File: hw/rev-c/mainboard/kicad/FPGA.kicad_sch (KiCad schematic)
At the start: 46 parts, among them J17 PMOD1, J18 PMOD2, J19 PROG, J4 BUS_EXPANSION, J9 FPGA_MCU, Q1 MMBT3904, SW3 CONFIG, U10 T8Q144C3

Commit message: hw: update more footprints
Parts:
- U10: footprint SnapEDA:QFP50P2200X2200X160-144N -> Package_QFP:LQFP-144_20x20mm_P0.5mm
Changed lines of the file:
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@@
 			)
 		)
-		(property "Footprint" "SnapEDA:QFP50P2200X2200X160-144N"
+		(property "Footprint" "Package_QFP:LQFP-144_20x20mm_P0.5mm"
 			(at 279.4 165.1 0)
 			(effects
@@
 			)
 		)
-		(property "Footprint" "SnapEDA:QFP50P2200X2200X160-144N"
+		(property "Footprint" "Package_QFP:LQFP-144_20x20mm_P0.5mm"
 			(at 180.34 149.86 0)
 			(effects
@@
 			)
 		)
-		(property "Footprint" "SnapEDA:QFP50P2200X2200X160-144N"
+		(property "Footprint" "Package_QFP:LQFP-144_20x20mm_P0.5mm"
 			(at 278.13 143.51 0)
 			(effects
@@
 			)
 		)
-		(property "Footprint" "SnapEDA:QFP50P2200X2200X160-144N"
+		(property "Footprint" "Package_QFP:LQFP-144_20x20mm_P0.5mm"
 			(at 181.61 107.95 0)
 			(effects
@@
 			)
 		)
-		(property "Footprint" "SnapEDA:QFP50P2200X2200X160-144N"
+		(property "Footprint" "Package_QFP:LQFP-144_20x20mm_P0.5mm"
 			(at 273.05 195.58 0)
 			(effects
@@
 			)
 		)
-		(property "Footprint" "SnapEDA:QFP50P2200X2200X160-144N"
+		(property "Footprint" "Package_QFP:LQFP-144_20x20mm_P0.5mm"
 			(at 180.34 124.46 0)
 			(effects
@@
 			)
 		)
-		(property "Footprint" "SnapEDA:QFP50P2200X2200X160-144N"
+		(property "Footprint" "Package_QFP:LQFP-144_20x20mm_P0.5mm"
 			(at 287.02 110.49 0)
 			(effects
@@
 			)
 		)
-		(property "Footprint" "SnapEDA:QFP50P2200X2200X160-144N"
+		(property "Footprint" "Package_QFP:LQFP-144_20x20mm_P0.5mm"
 			(at 276.86 88.9 0)
 			(effects
@@
 			)
 		)
-		(property "Footprint" "SnapEDA:QFP50P2200X2200X160-144N"
+		(property "Footprint" "Package_QFP:LQFP-144_20x20mm_P0.5mm"
 			(at 82.55 57.15 0)
 			(effects
@@
 			)
 		)
-		(property "Footprint" "SnapEDA:QFP50P2200X2200X160-144N"
+		(property "Footprint" "Package_QFP:LQFP-144_20x20mm_P0.5mm"
 			(at 180.34 93.98 0)
 			(effects
@@
 			)
 		)
-		(property "Footprint" "SnapEDA:QFP50P2200X2200X160-144N"
+		(property "Footprint" "Package_QFP:LQFP-144_20x20mm_P0.5mm"
 			(at 78.74 167.64 0)
 			(effects
@@
 			)
 		)
-		(property "Footprint" "SnapEDA:QFP50P2200X2200X160-144N"
+		(property "Footprint" "Package_QFP:LQFP-144_20x20mm_P0.5mm"
 			(at 177.8 181.61 0)
 			(effects
@@
 			)
 		)
-		(property "Footprint" "SnapEDA:QFP50P2200X2200X160-144N"
+		(property "Footprint" "Package_QFP:LQFP-144_20x20mm_P0.5mm"
 			(at 278.13 129.54 0)
 			(effects

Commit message: hw: rework buck converter (wip)
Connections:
- net HOLD: now reaches J19.15 (Pin_15)
- no-connect marks 0 -> 1
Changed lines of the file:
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@@
 		(color 0 0 0 0)
 	)
+	(no_connect
+		(at 168.91 41.91)
+	)
 	(bus_entry
 		(at 425.45 120.65)
@@
 	(wire
 		(pts
-			(xy 153.67 41.91) (xy 163.83 41.91)
+			(xy 153.67 41.91) (xy 168.91 41.91)
 		)
 		(stroke
@@
 		)
 	)
+	(label "HOLD"
+		(at 167.64 41.91 180)
+		(fields_autoplaced yes)
+		(effects
+			(font
+				(size 1.27 1.27)
+			)
+			(justify right bottom)
+		)
+	)
 	(label "PMOD2_3"
 		(at 375.92 2.54 180)
@@
 			)
 		)
-		(property "Datasheet" "https://datasheet.lcsc.com/lcsc/2304140030_Samsung-Electro-Mechanics-CL10A106MA8NRNC_C96446.pdf"
+		(property "Datasheet" "https://product.samsungsem.com/mlcc/CL10A106MA8NRN.do"
 			(at 229.87 50.8 0)
 			(effects
@@
 			)
 		)
-		(property "Datasheet" "https://datasheet.lcsc.com/lcsc/2304140030_Samsung-Electro-Mechanics-CL10A106MA8NRNC_C96446.pdf"
+		(property "Datasheet" "https://product.samsungsem.com/mlcc/CL10A106MA8NRN.do"
 			(at 477.52 93.98 0)
 			(effects
@@
 			)
 		)
-		(property "Datasheet" "https://datasheet.lcsc.com/lcsc/2304140030_Samsung-Electro-Mechanics-CL10A106MA8NRNC_C96446.pdf"
+		(property "Datasheet" "https://product.samsungsem.com/mlcc/CL10A106MA8NRN.do"
 			(at 401.32 13.97 0)
 			(effects
@@
 			)
 		)
-		(property "Datasheet" "https://datasheet.lcsc.com/lcsc/2304140030_Samsung-Electro-Mechanics-CL10A106MA8NRNC_C96446.pdf"
+		(property "Datasheet" "https://product.samsungsem.com/mlcc/CL10A106MA8NRN.do"
 			(at 440.69 96.52 0)
 			(effects
@@
 			)
 		)
-		(property "Datasheet" "https://datasheet.lcsc.com/lcsc/2304140030_Samsung-Electro-Mechanics-CL10A106MA8NRNC_C96446.pdf"
+		(property "Datasheet" "https://product.samsungsem.com/mlcc/CL10A106MA8NRN.do"
 			(at 336.55 13.97 0)
 			(effects

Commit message: hw: renumber reference designators
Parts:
- renumbered J19 to J5, J9 to J6, J17 to J7, J18 to J8, J4 to J9, R17 to R22, R18 to R23, R19 to R24, R20 to R25, R21 to R26, R22 to R27, RN9 to RN1, RN10 to RN2

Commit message: hw: match original PET designators for connectors
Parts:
- renumbered C38 to C39, C39 to C40, C40 to C41, C41 to C42, C42 to C43, C43 to C44, C44 to C45, C45 to C46, C46 to C47, C47 to C48, C48 to C49, C49 to C50, C50 to C51, C51 to C52, C52 to C53, C53 to C54, C54 to C55, C55 to C56, C56 to C57, C57 to C58, C58 to C59, C59 to C60, C60 to C61, C61 to C62, C62 to C63, C63 to C64, C64 to C65, C65 to C66, J7 to J17, J8 to J18, J5 to J22, J9 to J4, J6 to J9, R22 to R24, R23 to R25, R24 to R26, R25 to R27, R26 to R28, R27 to R29, RN2 to RN10, RN1 to RN9

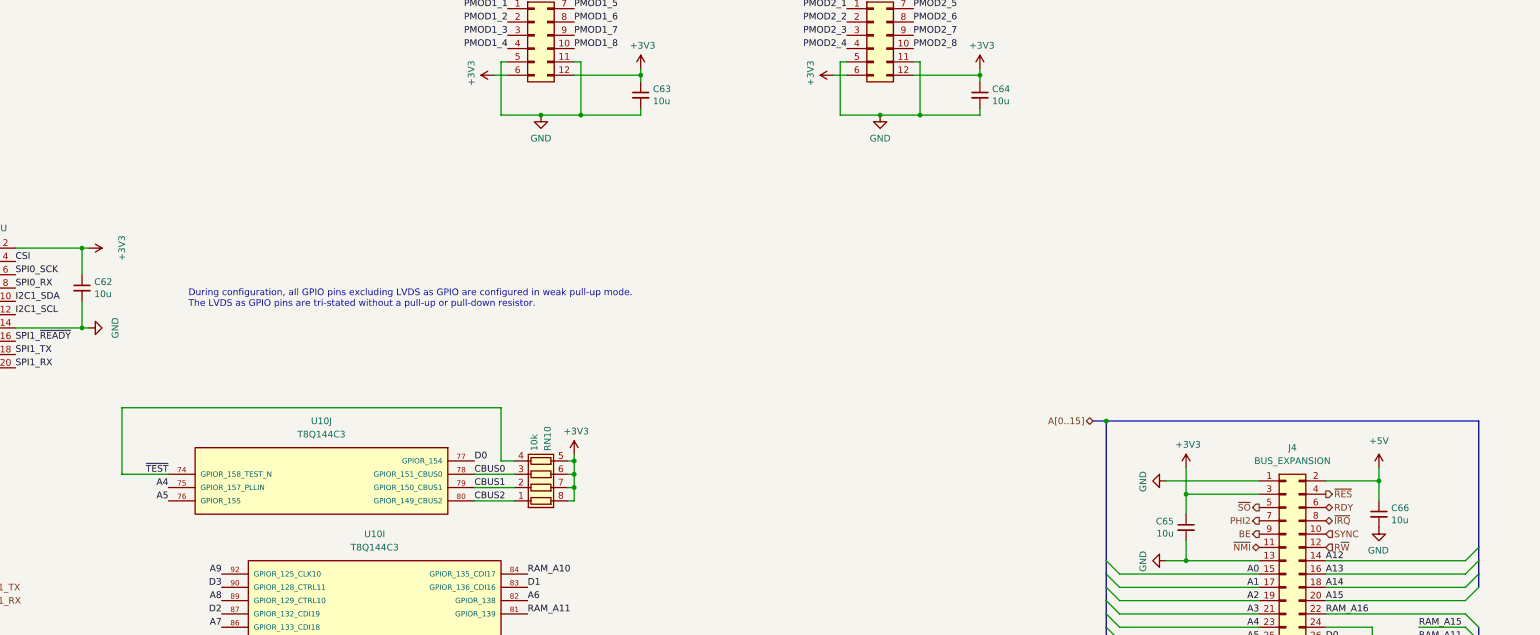
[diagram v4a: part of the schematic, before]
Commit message: hw: reduce some 3v3 decoupling caps to 4u7
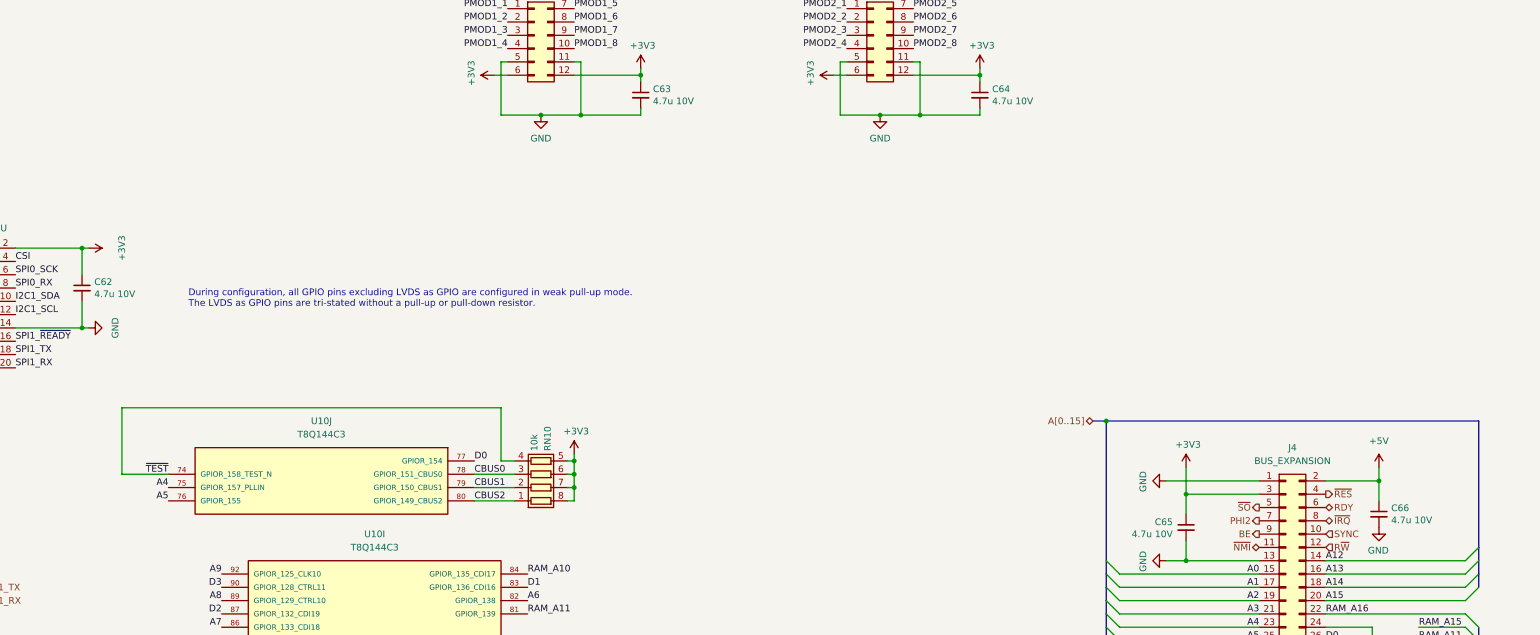
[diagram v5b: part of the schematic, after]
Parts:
- C62, C63, C64, C65, C66: value 10u -> 4.7u 10V; footprint Capacitor_SMD:C_0603_1608Metric -> Capacitor_SMD:C_0402_1005Metric; LCSC C96446 -> C23733

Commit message: hw: config can be solder jumper
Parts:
- SW3: footprint Button_Switch_THT:SW_DIP_SPSTx02_Slide_6.7x6.64mm_W7.62mm_P2.54mm_LowProfile -> EconoPET:SW_DIP_SPSTx02_Slide_6.7x6.64mm_W7.62mm_P2.54mm_LowProfile_or_SolderJumper
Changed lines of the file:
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@@
 			)
 		)
-		(property "Footprint" "Button_Switch_THT:SW_DIP_SPSTx02_Slide_6.7x6.64mm_W7.62mm_P2.54mm_LowProfile"
+		(property "Footprint" "EconoPET:SW_DIP_SPSTx02_Slide_6.7x6.64mm_W7.62mm_P2.54mm_LowProfile_or_SolderJumper"
 			(at 386.08 194.31 0)
 			(effects

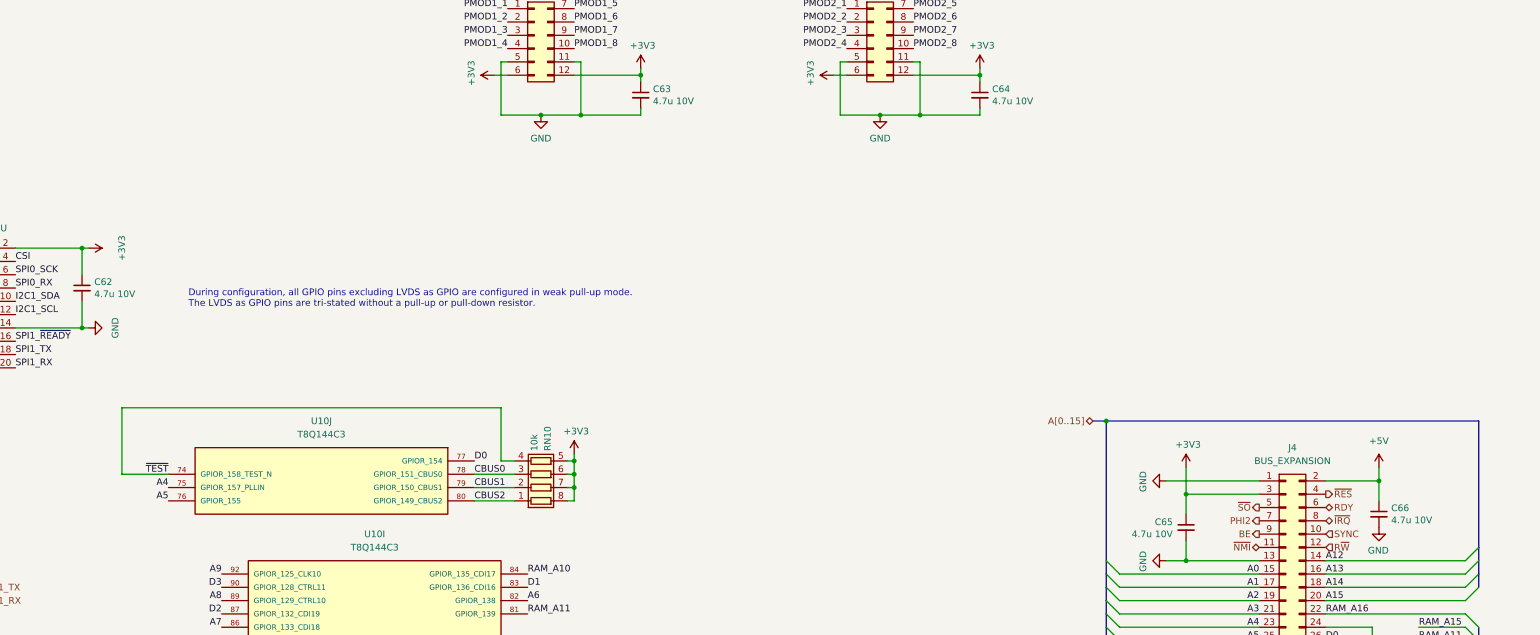
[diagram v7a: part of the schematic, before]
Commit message: hw: routing touchups, killer poke mitigation
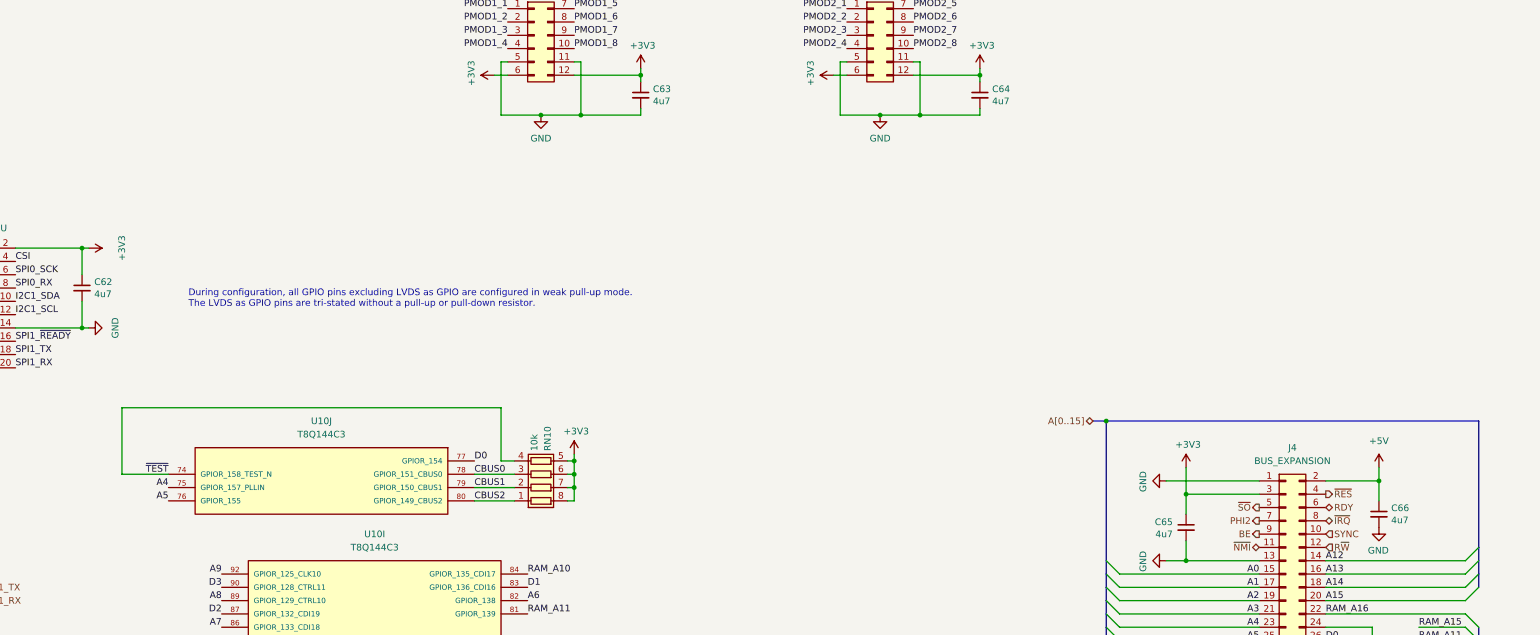
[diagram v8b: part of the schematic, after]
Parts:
- C62, C63, C64, C65, C66: value 4.7u 10V -> 4u7; LCSC C23733 -> C1538
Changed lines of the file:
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@@
 			)
 		)
-		(property "Value" "4.7u 10V"
+		(property "Value" "4u7"
 			(at 438.15 97.79 0)
 			(effects
@@
 			)
 		)
-		(property "Datasheet" "https://product.samsungsem.com/mlcc/CL05A475MP5NRN.do"
+		(property "Datasheet" "https://www.lcsc.com/datasheet/lcsc_datasheet_2304140030_FH--Guangdong-Fenghua-Advanced-Tech-0402B472K500NT_C1538.pdf"
 			(at 440.69 96.52 0)
 			(effects
@@
 			)
 		)
-		(property "LCSC" "C23733"
+		(property "LCSC" "C1538"
 			(at 440.69 96.52 0)
 			(effects
@@
 			)
 		)
-		(property "Value" "4.7u 10V"
+		(property "Value" "4u7"
 			(at 232.2068 51.943 0)
 			(effects
@@
 			)
 		)
-		(property "Datasheet" "https://product.samsungsem.com/mlcc/CL05A475MP5NRN.do"
+		(property "Datasheet" "https://www.lcsc.com/datasheet/lcsc_datasheet_2304140030_FH--Guangdong-Fenghua-Advanced-Tech-0402B472K500NT_C1538.pdf"
 			(at 229.87 50.8 0)
 			(effects
@@
 			)
 		)
-		(property "LCSC" "C23733"
+		(property "LCSC" "C1538"
 			(at 229.87 50.8 0)
 			(effects
@@
 			)
 		)
-		(property "Value" "4.7u 10V"
+		(property "Value" "4u7"
 			(at 479.8568 95.123 0)
 			(effects
@@
 			)
 		)
-		(property "Datasheet" "https://product.samsungsem.com/mlcc/CL05A475MP5NRN.do"
+		(property "Datasheet" "https://www.lcsc.com/datasheet/lcsc_datasheet_2304140030_FH--Guangdong-Fenghua-Advanced-Tech-0402B472K500NT_C1538.pdf"
 			(at 477.52 93.98 0)
 			(effects
@@
 			)
 		)
-		(property "LCSC" "C23733"
+		(property "LCSC" "C1538"
 			(at 477.52 93.98 0)
 			(effects
@@
 			)
 		)
-		(property "Value" "4.7u 10V"
+		(property "Value" "4u7"
 			(at 338.8868 15.113 0)
 			(effects
@@
 			)
 		)
-		(property "Datasheet" "https://product.samsungsem.com/mlcc/CL05A475MP5NRN.do"
+		(property "Datasheet" "https://www.lcsc.com/datasheet/lcsc_datasheet_2304140030_FH--Guangdong-Fenghua-Advanced-Tech-0402B472K500NT_C1538.pdf"
 			(at 336.55 13.97 0)
 			(effects
@@
 			)
 		)
-		(property "LCSC" "C23733"
+		(property "LCSC" "C1538"
 			(at 336.55 13.97 0)
 			(effects
@@
 			)
 		)
-		(property "Value" "4.7u 10V"
+		(property "Value" "4u7"
 			(at 403.6568 15.113 0)
 			(effects
@@
 			)
 		)
-		(property "Datasheet" "https://product.samsungsem.com/mlcc/CL05A475MP5NRN.do"
+		(property "Datasheet" "https://www.lcsc.com/datasheet/lcsc_datasheet_2304140030_FH--Guangdong-Fenghua-Advanced-Tech-0402B472K500NT_C1538.pdf"
 			(at 401.32 13.97 0)
 			(effects
@@
 			)
 		)
-		(property "LCSC" "C23733"
+		(property "LCSC" "C1538"
 			(at 401.32 13.97 0)
 			(effects
